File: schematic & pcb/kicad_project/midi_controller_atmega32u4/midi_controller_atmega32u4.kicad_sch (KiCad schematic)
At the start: 18 parts, among them J1 ANAL-MDL, SW1 OCT+, SW2 OCT-, U1 ProMicro, U2 DM-OLED096-636

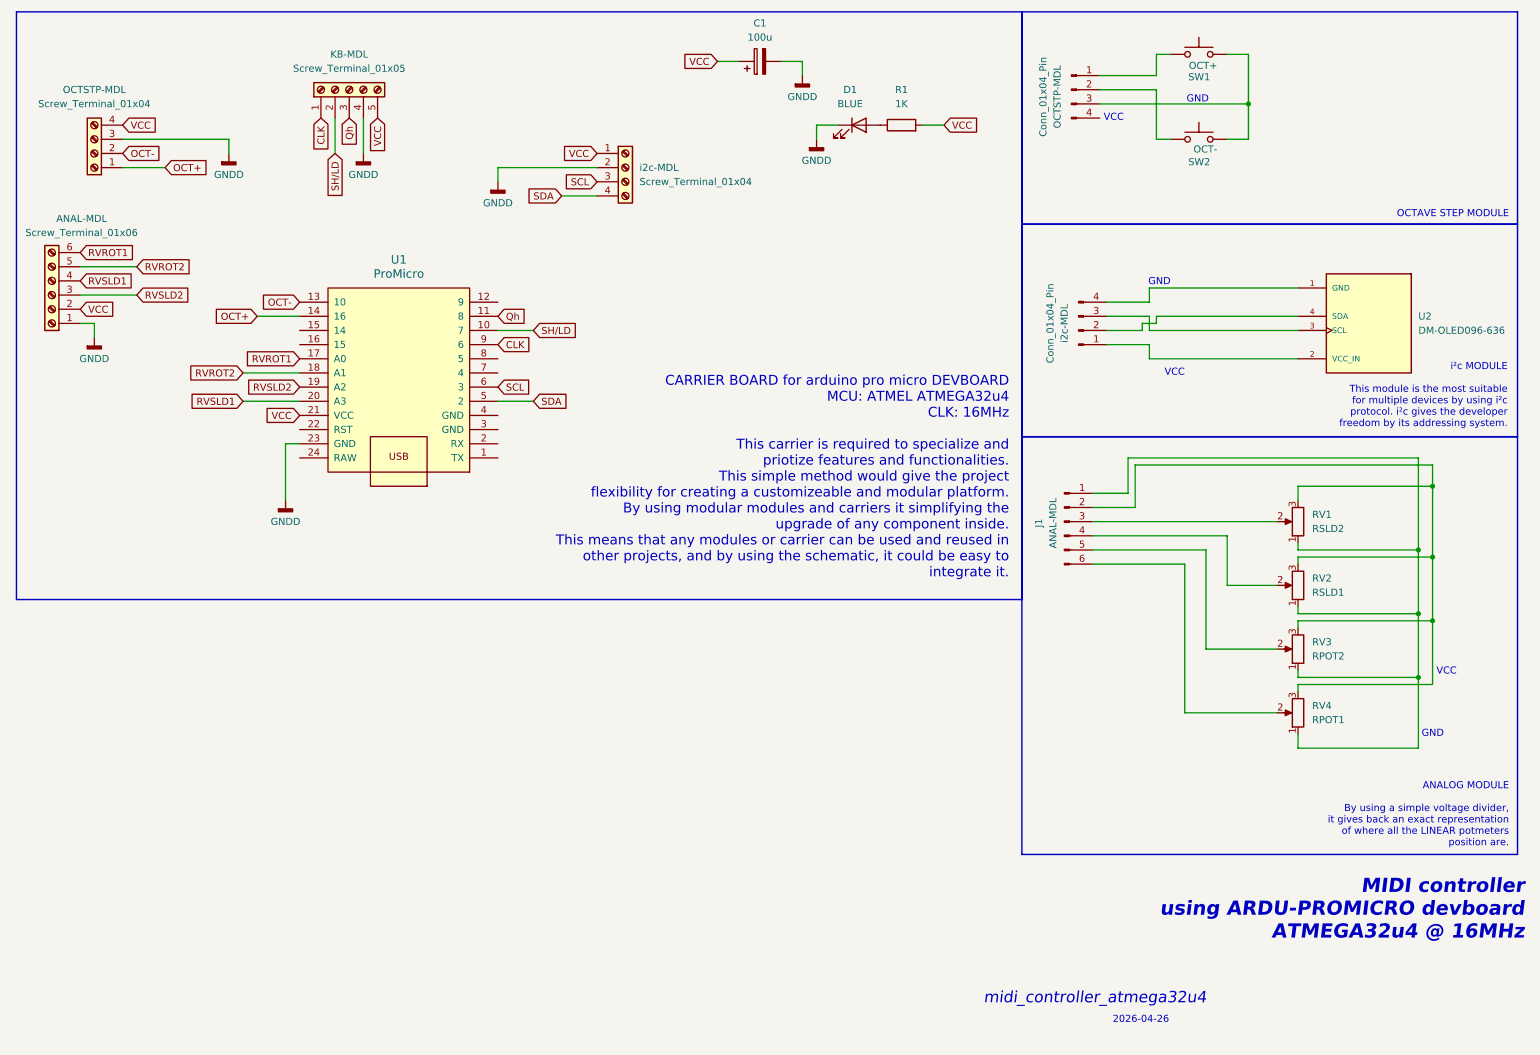
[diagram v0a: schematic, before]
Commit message: SCHEMATIC UPDATE 2026-04-27
 - kapcsolási rajz frissítve (keyboard)
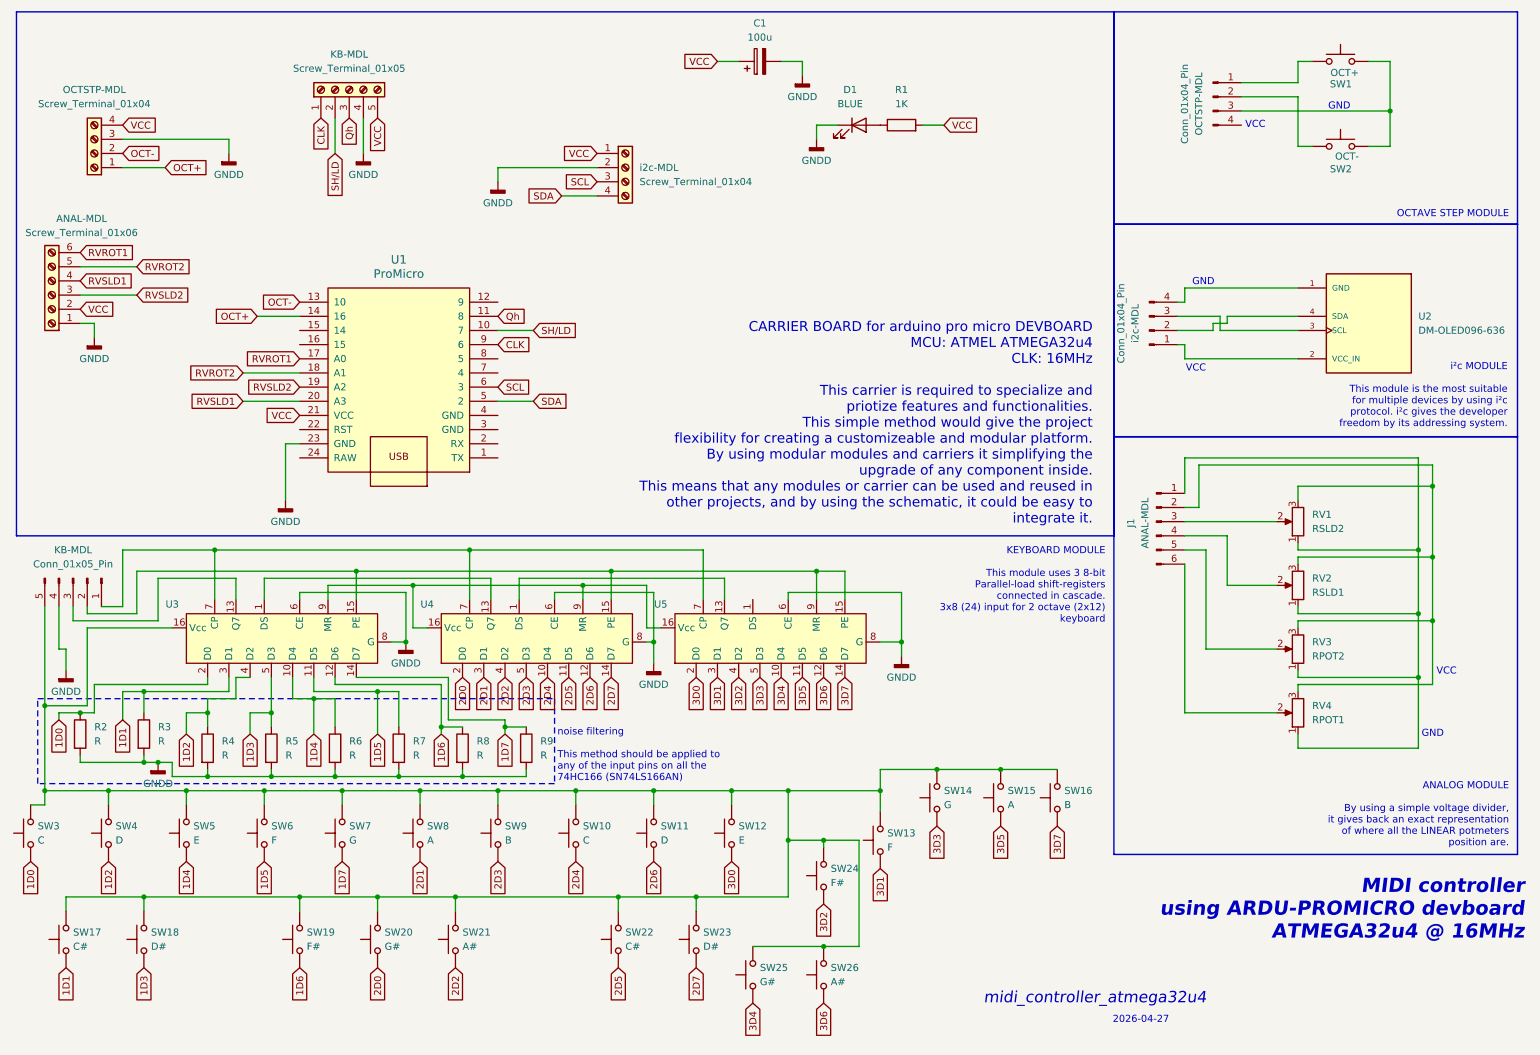
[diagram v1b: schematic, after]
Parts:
- added KB-MDL: Conn_01x05_Pin, symbol Connector:Conn_01x05_Pin
- added R2, R3, R4, R5, R6, R7, R8, R9: R, symbol Device:R
- added SW10, SW3: C, symbol Switch:SW_Push
- added SW11, SW4: D, symbol Switch:SW_Push
- added SW12, SW5: E, symbol Switch:SW_Push
- added SW13, SW6: F, symbol Switch:SW_Push
- added SW14, SW7: G, symbol Switch:SW_Push
- added SW15, SW8: A, symbol Switch:SW_Push
- added SW16, SW9: B, symbol Switch:SW_Push
- added SW17, SW22: C#, symbol Switch:SW_Push
- added SW18, SW23: D#, symbol Switch:SW_Push
- added SW19, SW24: F#, symbol Switch:SW_Push
- added SW20, SW25: G#, symbol Switch:SW_Push
- added SW21, SW26: A#, symbol Switch:SW_Push
- added U3, U4, U5: ~, symbol custom:74HC166
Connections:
- net GNDD: now also KB-MDL.4 (Pin_4), R2.2, R3.2, R4.2, R5.2, R6.2, R7.2, R8.2, R9.2, U3.6 (CE), U3.8 (G), U4.6 (CE), U4.8 (G), U5.6 (CE), U5.8 (G)
- new net: KB-MDL.5 (Pin_5), SW10.2, SW11.2, SW12.2, SW13.2, SW14.2, SW15.2, SW16.2, SW17.2, SW18.2, SW19.2, SW20.2, SW21.2, SW22.2, SW23.2, SW24.2, SW25.2, SW26.2, SW3.2, SW4.2, SW5.2, SW6.2, SW7.2, SW8.2, SW9.2, U3.16 (Vcc)
- new net: KB-MDL.1 (Pin_1), U3.7 (CP), U4.7 (CP), U5.7 (CP)
- new net: KB-MDL.2 (Pin_2), U3.15 (PE), U4.15 (PE), U5.15 (PE), U5.9 (MR)
- new net: KB-MDL.3 (Pin_3), U3.13 (Q7)
- new net: U4.1 (DS), U5.13 (Q7)
- new net: U3.1 (DS), U4.13 (Q7)
- new net: U3.9 (MR), U4.16 (Vcc), U4.9 (MR), U5.16 (Vcc)
- new net 1D0: R2.1, SW3.1, U3.2 (D0)
- new net 1D1: R3.1, SW17.1, U3.3 (D1)
- new net 1D2: R4.1, SW4.1, U3.4 (D2)
- new net 1D3: R5.1, SW18.1, U3.5 (D3)
- new net 1D4: R6.1, SW5.1, U3.10 (D4)
- new net 1D5: R7.1, SW6.1, U3.11 (D5)
- new net 1D6: R8.1, SW19.1, U3.12 (D6)
- new net 1D7: R9.1, SW7.1, U3.14 (D7)
- new net 2D0: SW20.1, U4.2 (D0)
- new net 2D1: SW8.1, U4.3 (D1)
- new net 2D2: SW21.1, U4.4 (D2)
- new net 2D3: SW9.1, U4.5 (D3)
- new net 2D4: SW10.1, U4.10 (D4)
- new net 2D5: SW22.1, U4.11 (D5)
- new net 2D6: SW11.1, U4.12 (D6)
- new net 2D7: SW23.1, U4.14 (D7)
- new net 3D0: SW12.1, U5.2 (D0)
- new net 3D1: SW13.1, U5.3 (D1)
- new net 3D2: SW24.1, U5.4 (D2)
- new net 3D3: SW14.1, U5.5 (D3)
- new net 3D4: SW25.1, U5.10 (D4)
- new net 3D5: SW15.1, U5.11 (D5)
- new net 3D6: SW26.1, U5.12 (D6)
- new net 3D7: SW16.1, U5.14 (D7)
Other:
- note added: "2026-04-27"
- note added: "KEYBOARD MODULE This module uses 3 8-bit Parallel-load shift-registers connected in cascade. 3x8 (24) input for 2 octave (2x12) keyboard"
- note added: "noise filtering This method should be applied to any of the input pins on all the 74HC166 (SN74LS166AN)"
- note removed: "2026-04-26"
- moved on the sheet: J1, OCTSTP-MDL, SW1, SW2, i2c-MDL
